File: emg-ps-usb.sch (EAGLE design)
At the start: 13 parts, among them U2 PHONE_JACK_MONO, X1 53047-04

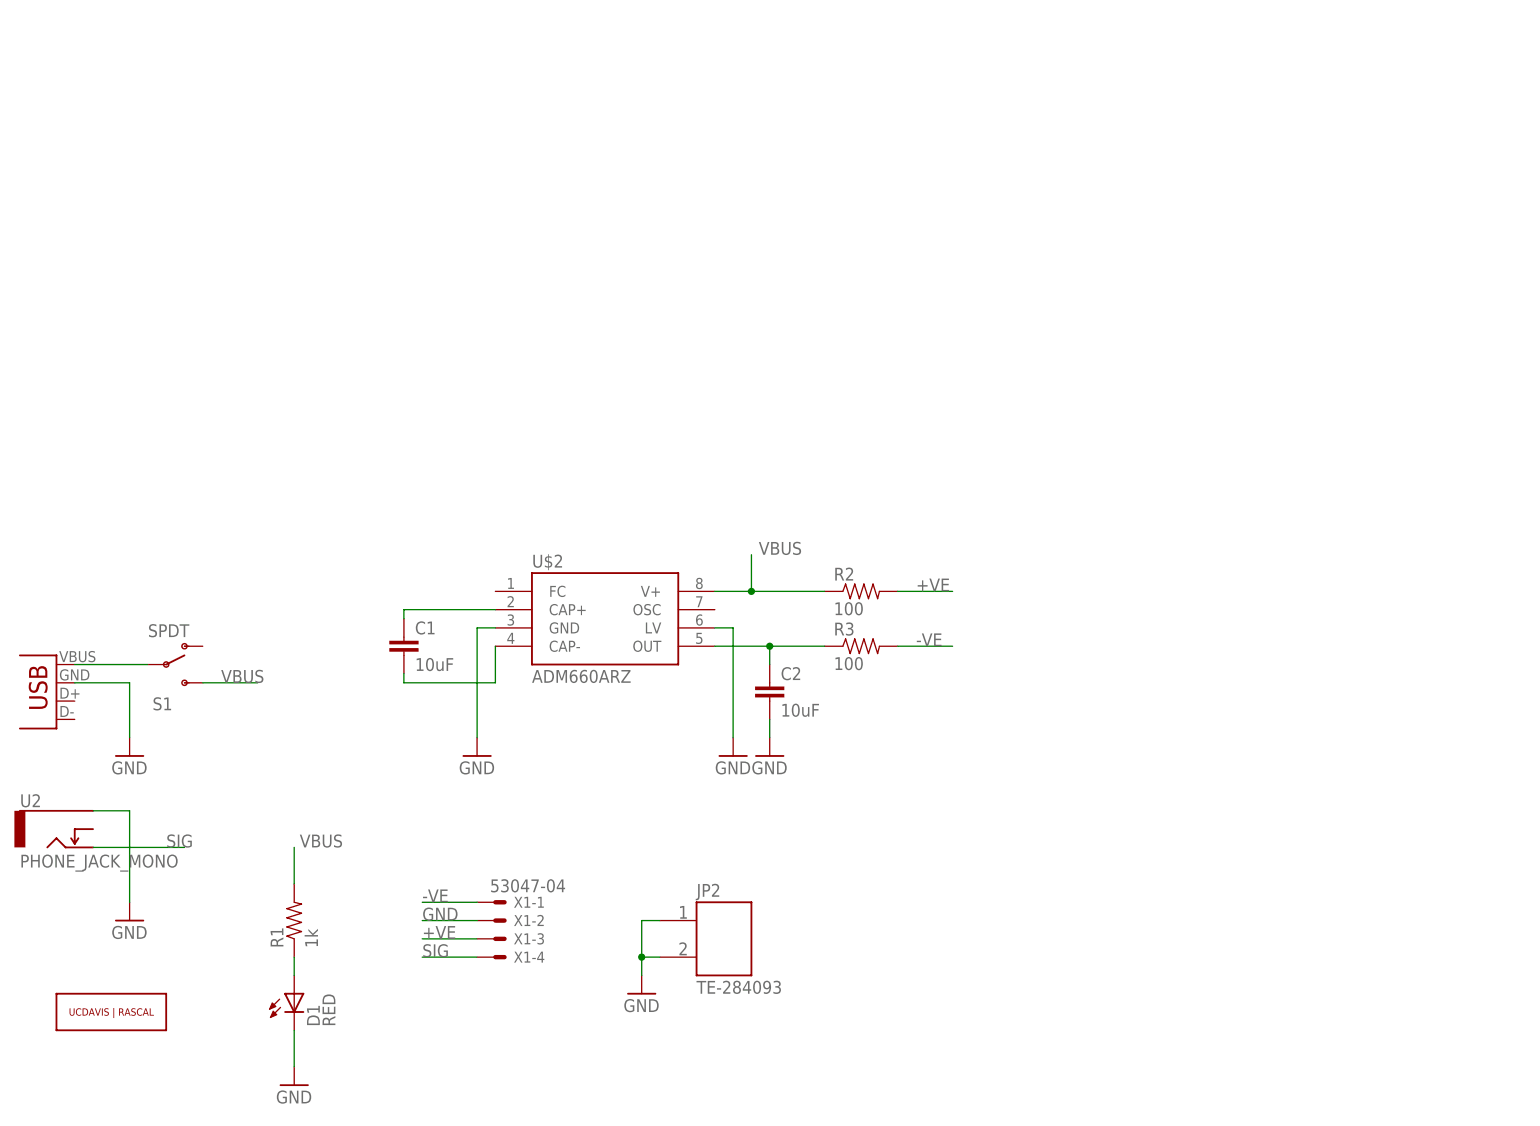
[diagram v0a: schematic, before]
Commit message: Cleaned up schematic and added a frame.
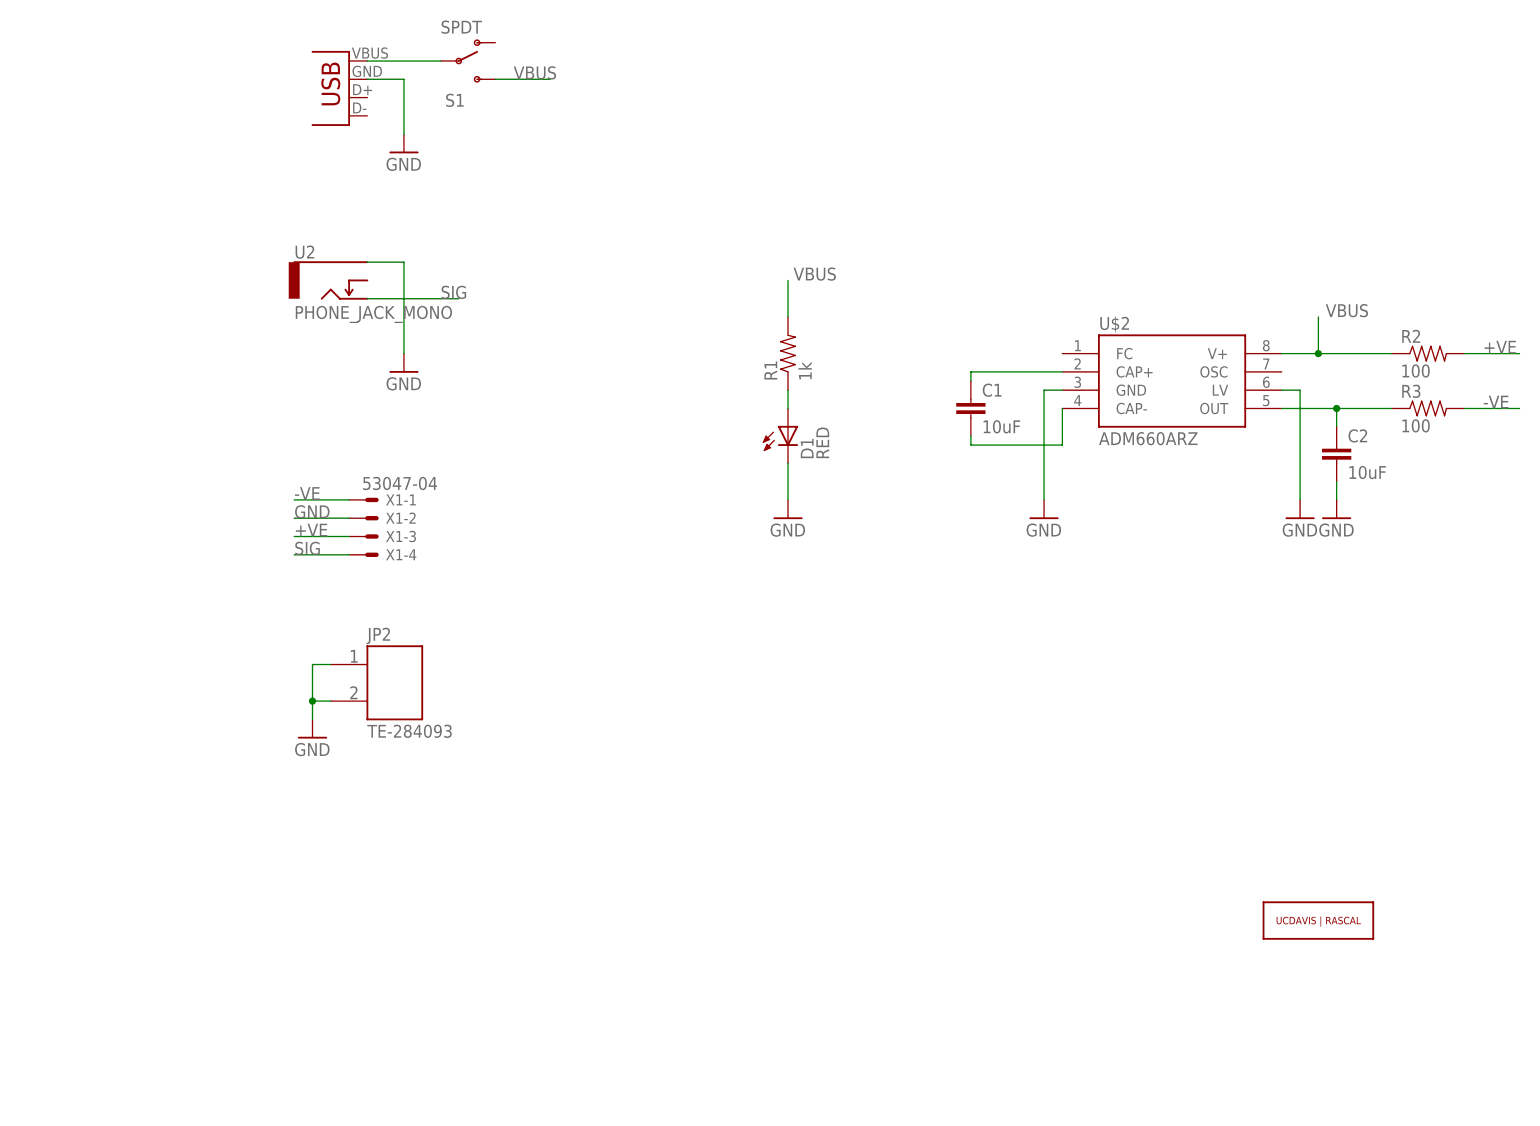
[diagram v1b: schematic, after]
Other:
- moved on the sheet: C1, C2, D1, JP2, R1, R2, R3, S1, U$2, U2, X1-1, X1-2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

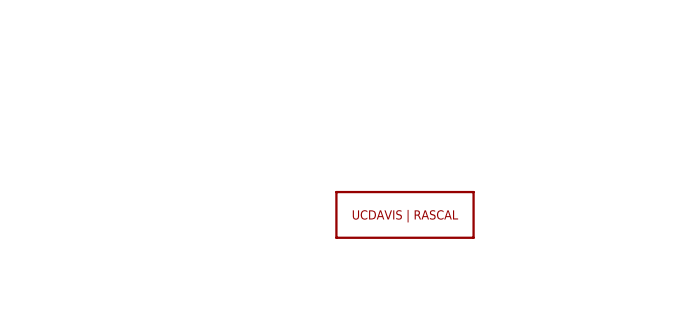
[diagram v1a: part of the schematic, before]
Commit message: Now using EMG amp outline and UCDAVIS|RASCAL logo from ucdrascal-eagle-lib.
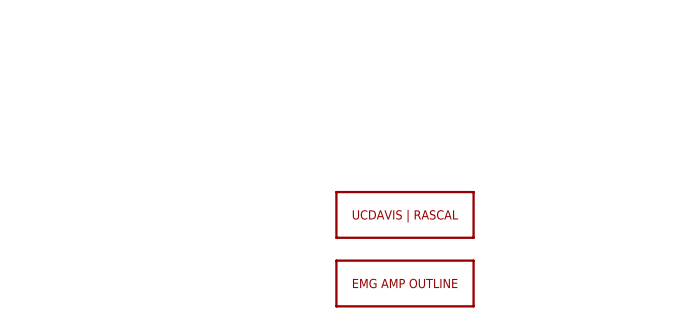
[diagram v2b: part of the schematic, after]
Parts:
- added U$3: EMG_AMP_OUTLINE-Y03ENDS, ucdrascal-eagle-lib:EMG_AMP_OUTLINE-Y03ENDS
- U$1: value UCDAVIS-RASCAL_LOGO -> UCDAVIS-RASCAL_LOGO-2LINE; device eagle-lib:UCDAVIS-RASCAL_LOGO -> ucdrascal-eagle-lib:UCDAVIS-RASCAL_LOGO-2LINE
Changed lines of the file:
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@@
 <setting verticaltext="up"/>
 </settings>
-<grid distance="0.1" unitdist="inch" unit="inch" style="lines" multiple="1" display="yes" altdistance="0.01" altunitdist="inch" altunit="inch"/>
+<grid distance="0.1" unitdist="inch" unit="inch" style="lines" multiple="1" display="no" altdistance="0.01" altunitdist="inch" altunit="inch"/>
 <layers>
 <layer number="1" name="Top" color="4" fill="1" visible="no" active="no"/>
@@
 <part name="GND6" library="SparkFun-Aesthetics" deviceset="GND" device=""/>
 <part name="GND7" library="SparkFun-Aesthetics" deviceset="GND" device=""/>
-<part name="U$1" library="eagle-lib" deviceset="UCDAVIS-RASCAL_LOGO" device=""/>
 <part name="FRAME1" library="frames" deviceset="A4L-LOC" device=""/>
+<part name="U$1" library="ucdrascal-eagle-lib" deviceset="UCDAVIS-RASCAL_LOGO" device="-2LINE"/>
+<part name="U$3" library="ucdrascal-eagle-lib" deviceset="EMG_AMP_OUTLINE" device="-Y03ENDS"/>
 </parts>
 <sheets>
@@
 <instance part="GND6" gate="1" x="134.62" y="73.66"/>
 <instance part="GND7" gate="1" x="33.02" y="43.18"/>
+<instance part="FRAME1" gate="G$1" x="0" y="0"/>
 <instance part="U$1" gate="G$1" x="172.72" y="17.78"/>
-<instance part="FRAME1" gate="G$1" x="0" y="0"/>
+<instance part="U$3" gate="G$1" x="172.72" y="10.16"/>
 </instances>
 <busses>

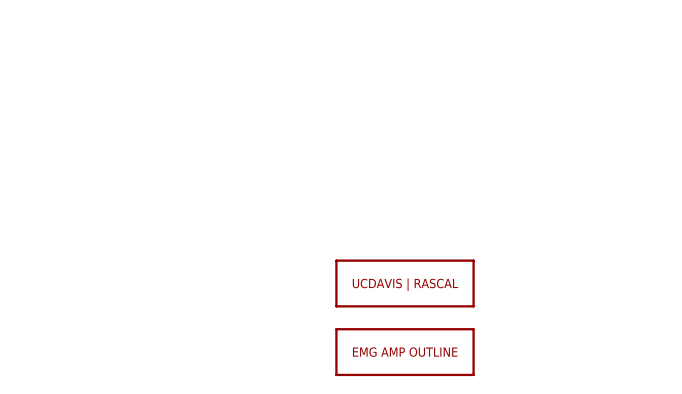
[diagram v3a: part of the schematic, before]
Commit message: Cleaned up layout and routing. Moved LED to top and removed UCDRASCAL logo.
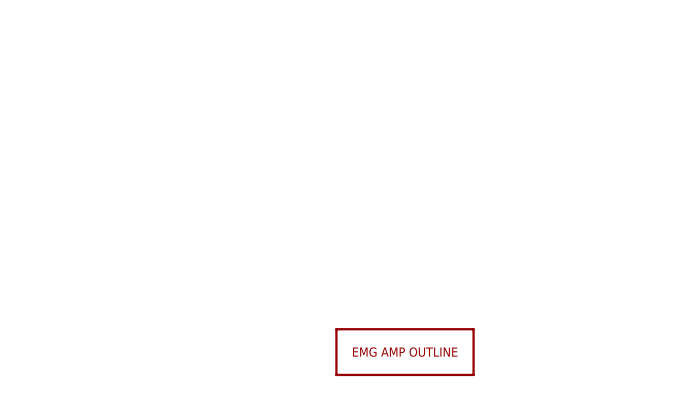
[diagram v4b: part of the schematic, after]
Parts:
- removed U$1: UCDAVIS-RASCAL_LOGO-2LINE, ucdrascal-eagle-lib:UCDAVIS-RASCAL_LOGO-2LINE
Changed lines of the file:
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@@
 <part name="GND7" library="SparkFun-Aesthetics" deviceset="GND" device=""/>
 <part name="FRAME1" library="frames" deviceset="A4L-LOC" device=""/>
-<part name="U$1" library="ucdrascal-eagle-lib" deviceset="UCDAVIS-RASCAL_LOGO" device="-2LINE"/>
 <part name="U$3" library="ucdrascal-eagle-lib" deviceset="EMG_AMP_OUTLINE" device="-Y03ENDS"/>
 </parts>
@@
 <instance part="GND7" gate="1" x="33.02" y="43.18"/>
 <instance part="FRAME1" gate="G$1" x="0" y="0"/>
-<instance part="U$1" gate="G$1" x="172.72" y="17.78"/>
 <instance part="U$3" gate="G$1" x="172.72" y="10.16"/>
 </instances>

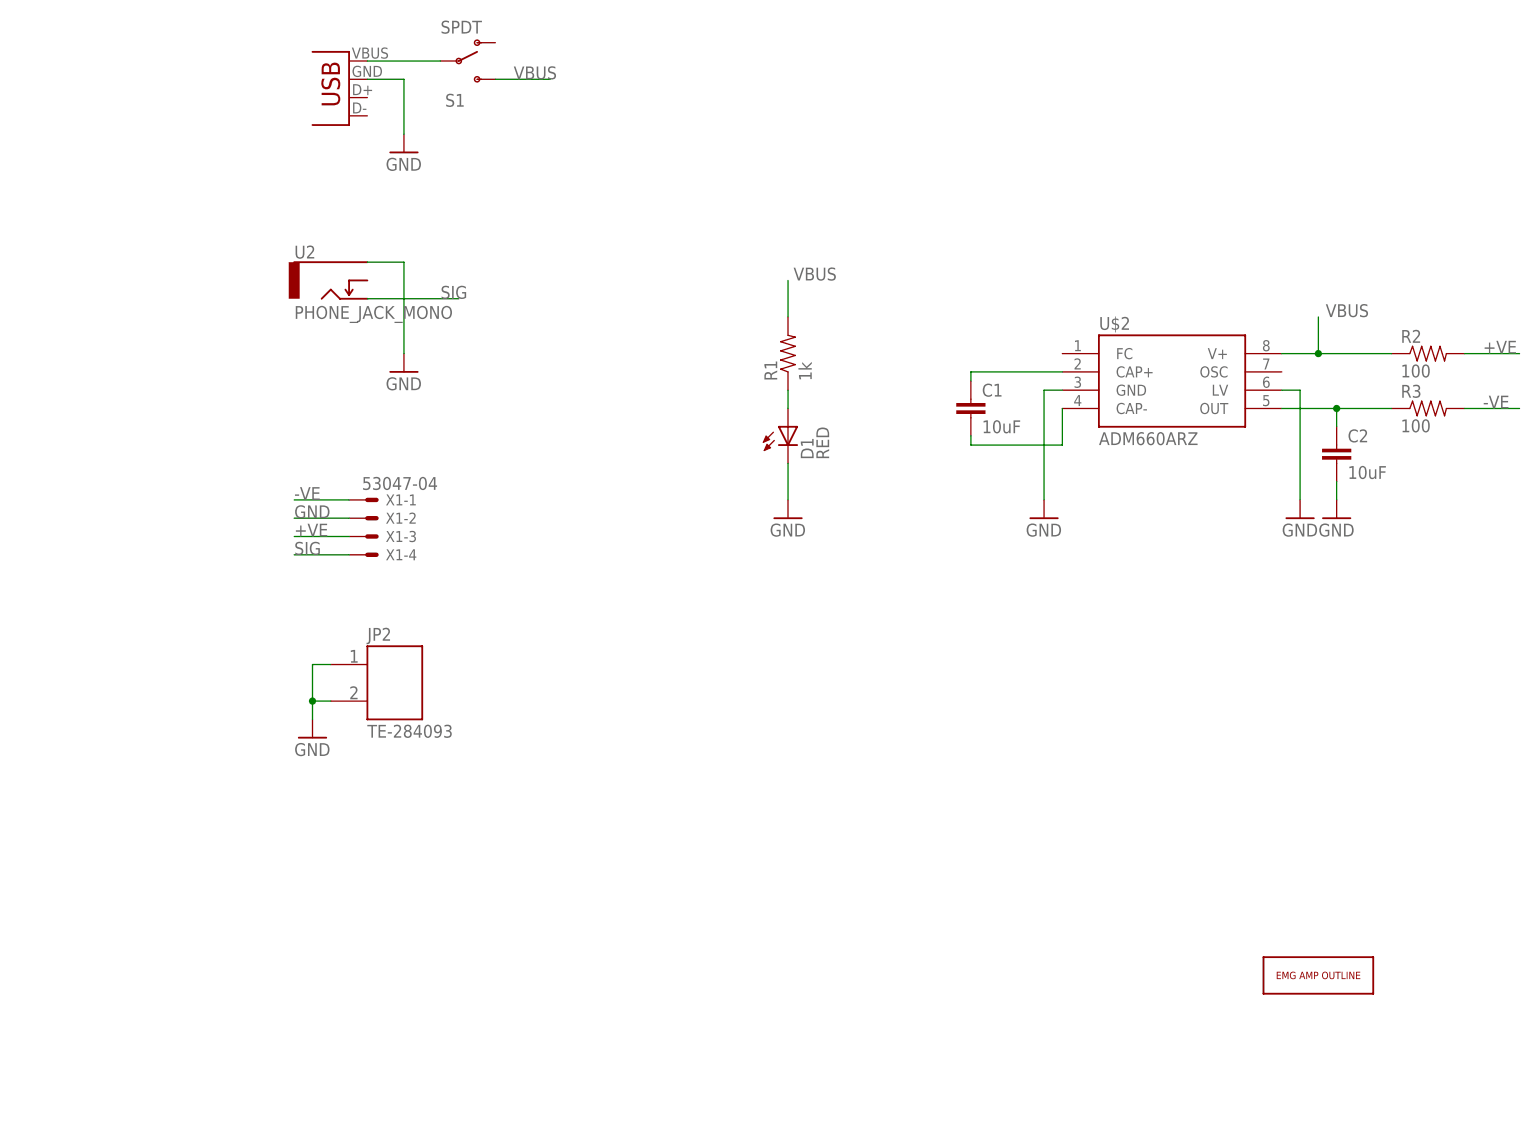
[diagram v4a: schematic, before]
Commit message: Added UCDRASCAL logo. Swapped the 4x1 Molex connector for just a wire to board interface. Updated BOM.
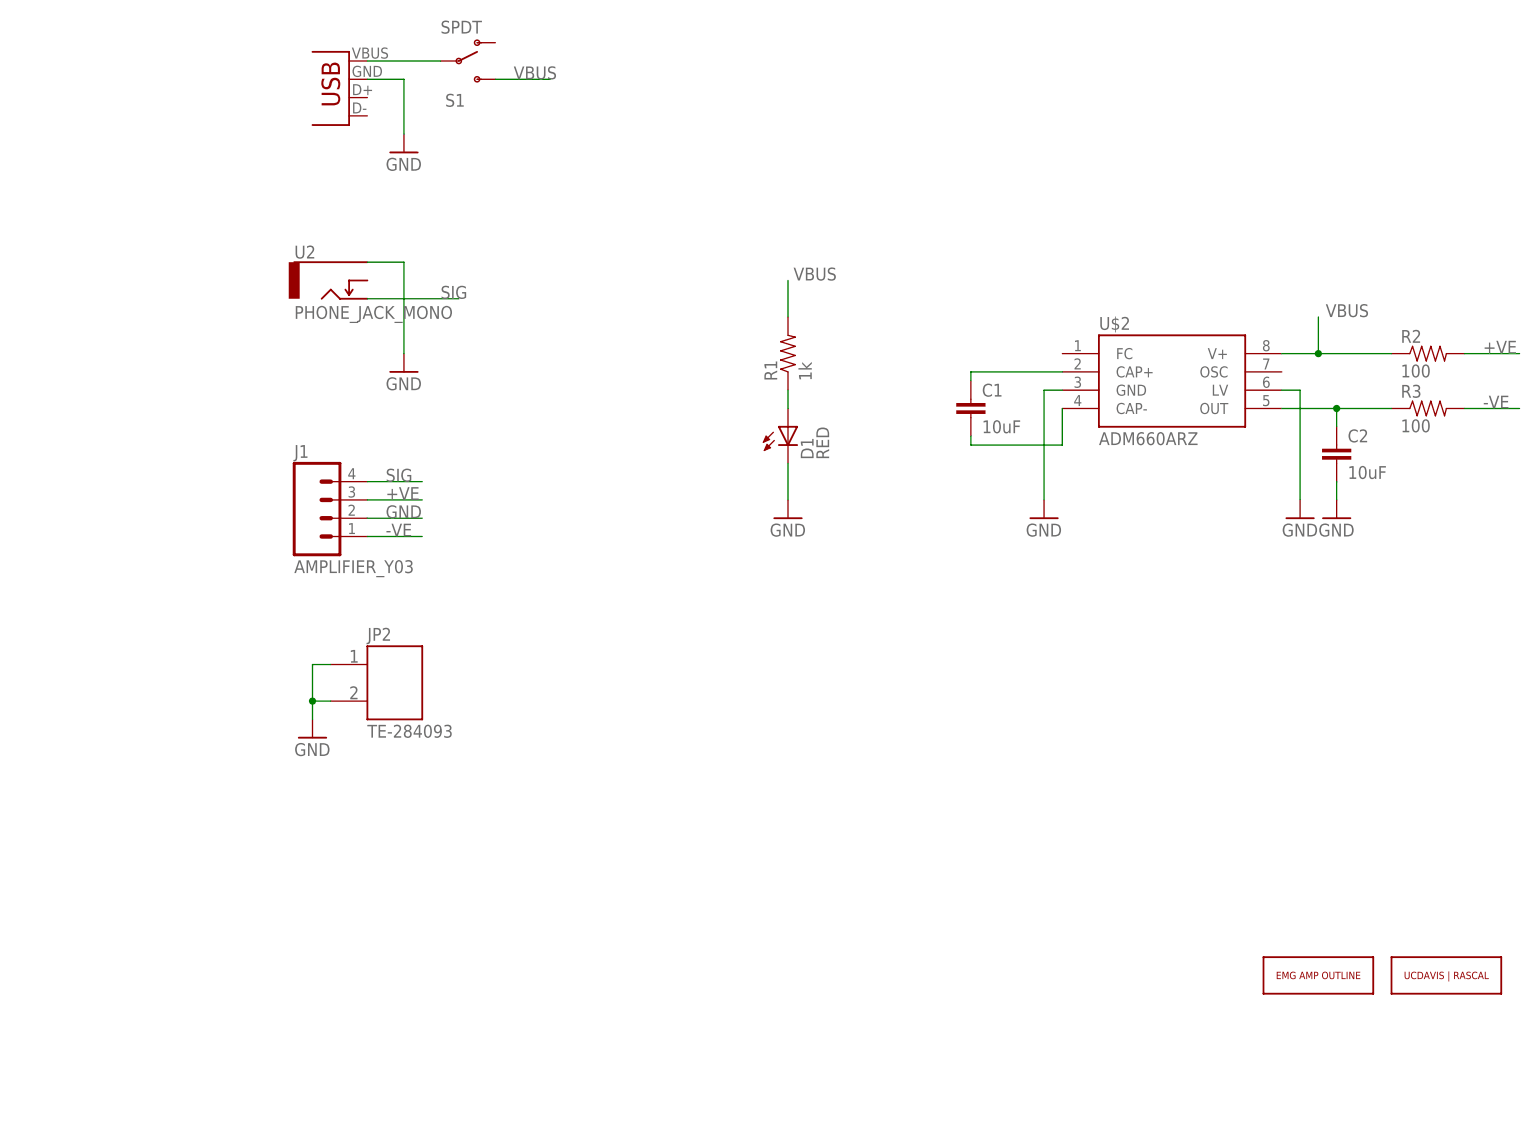
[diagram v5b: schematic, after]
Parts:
- removed X1: 53047-04, con-molex:53047-04
- added J1: AMPLIFIER_Y03, eagle-lib:AMPLIFIER_Y03
- added U$1: UCDAVIS-RASCAL_LOGO-2LINE, ucdrascal-eagle-lib:UCDAVIS-RASCAL_LOGO-2LINE
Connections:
- net +VE: now also J1.3; no longer X1-3.S
- net -VE: now also J1.1; no longer X1-1.S
- net GND: now also J1.2; no longer X1-2.S
- net SIG: now also J1.4; no longer X1-4.S
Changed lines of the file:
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@@
 <part name="R2" library="SparkFun-Resistors" deviceset="RESISTOR" device="0805-RES" value="100"/>
 <part name="R3" library="SparkFun-Resistors" deviceset="RESISTOR" device="0805-RES" value="100"/>
-<part name="X1" library="con-molex" deviceset="53?-04" device="047"/>
 <part name="JP2" library="eagle-lib" deviceset="TE-284093" device=""/>
 <part name="S1" library="SparkFun-Electromechanical" deviceset="SWITCH-SPDT" device="-SMD-A" value="SPDT"/>
@@
 <part name="FRAME1" library="frames" deviceset="A4L-LOC" device=""/>
 <part name="U$3" library="ucdrascal-eagle-lib" deviceset="EMG_AMP_OUTLINE" device="-Y03ENDS"/>
+<part name="J1" library="eagle-lib" deviceset="AMPLIFIER_Y03" device=""/>
+<part name="U$1" library="ucdrascal-eagle-lib" deviceset="UCDAVIS-RASCAL_LOGO" device="-2LINE"/>
 </parts>
 <sheets>
@@
 <instance part="R2" gate="G$1" x="187.96" y="96.52"/>
 <instance part="R3" gate="G$1" x="187.96" y="88.9"/>
-<instance part="X1" gate="-1" x="40.64" y="76.2"/>
-<instance part="X1" gate="-2" x="40.64" y="73.66"/>
-<instance part="X1" gate="-3" x="40.64" y="71.12"/>
-<instance part="X1" gate="-4" x="40.64" y="68.58"/>
 <instance part="JP2" gate="G$1" x="43.18" y="50.8"/>
 <instance part="S1" gate="1" x="53.34" y="137.16"/>
@@
 <instance part="FRAME1" gate="G$1" x="0" y="0"/>
 <instance part="U$3" gate="G$1" x="172.72" y="10.16"/>
+<instance part="J1" gate="G$1" x="35.56" y="76.2"/>
+<instance part="U$1" gate="G$1" x="190.5" y="10.16"/>
 </instances>
 <busses>
@@
 <wire x1="137.16" y1="91.44" x2="134.62" y2="91.44" width="0.1524" layer="91"/>
 <wire x1="134.62" y1="91.44" x2="134.62" y2="76.2" width="0.1524" layer="91"/>
-</segment>
-<segment>
-<pinref part="X1" gate="-2" pin="S"/>
-<wire x1="38.1" y1="73.66" x2="30.48" y2="73.66" width="0.1524" layer="91"/>
-<label x="30.48" y="73.66" size="1.778" layer="95"/>
 </segment>
 <segment>
@@
 <junction x="33.02" y="48.26"/>
 </segment>
+<segment>
+<pinref part="J1" gate="G$1" pin="2"/>
+<wire x1="40.64" y1="73.66" x2="48.26" y2="73.66" width="0.1524" layer="91"/>
+<label x="43.18" y="73.66" size="1.778" layer="95"/>
+</segment>
 </net>
 <net name="VBUS" class="0">
@@
 </segment>
 <segment>
-<pinref part="X1" gate="-4" pin="S"/>
-<wire x1="38.1" y1="68.58" x2="30.48" y2="68.58" width="0.1524" layer="91"/>
-<label x="30.48" y="68.58" size="1.778" layer="95"/>
+<pinref part="J1" gate="G$1" pin="4"/>
+<wire x1="40.64" y1="78.74" x2="48.26" y2="78.74" width="0.1524" layer="91"/>
+<label x="43.18" y="78.74" size="1.778" layer="95"/>
 </segment>
 </net>
@@
 </segment>
 <segment>
-<pinref part="X1" gate="-3" pin="S"/>
-<wire x1="38.1" y1="71.12" x2="30.48" y2="71.12" width="0.1524" layer="91"/>
-<label x="30.48" y="71.12" size="1.778" layer="95"/>
+<pinref part="J1" gate="G$1" pin="3"/>
+<wire x1="40.64" y1="76.2" x2="48.26" y2="76.2" width="0.1524" layer="91"/>
+<label x="43.18" y="76.2" size="1.778" layer="95"/>
 </segment>
 </net>
@@
 </segment>
 <segment>
-<pinref part="X1" gate="-1" pin="S"/>
-<wire x1="38.1" y1="76.2" x2="30.48" y2="76.2" width="0.1524" layer="91"/>
-<label x="30.48" y="76.2" size="1.778" layer="95"/>
+<pinref part="J1" gate="G$1" pin="1"/>
+<wire x1="40.64" y1="71.12" x2="48.26" y2="71.12" width="0.1524" layer="91"/>
+<label x="43.18" y="71.12" size="1.778" layer="95"/>
 </segment>
 </net>
@@
 </sheet>
 </sheets>
+<errors>
+</errors>
 </schematic>
 </drawing>
